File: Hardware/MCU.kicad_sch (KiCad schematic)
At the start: 30 parts, among them IC1 SN74AHC1G32DBVR, J3 SWD, SW1 RST, SW2 BOOT, U5 STM32L431CBTx, Y1 8M

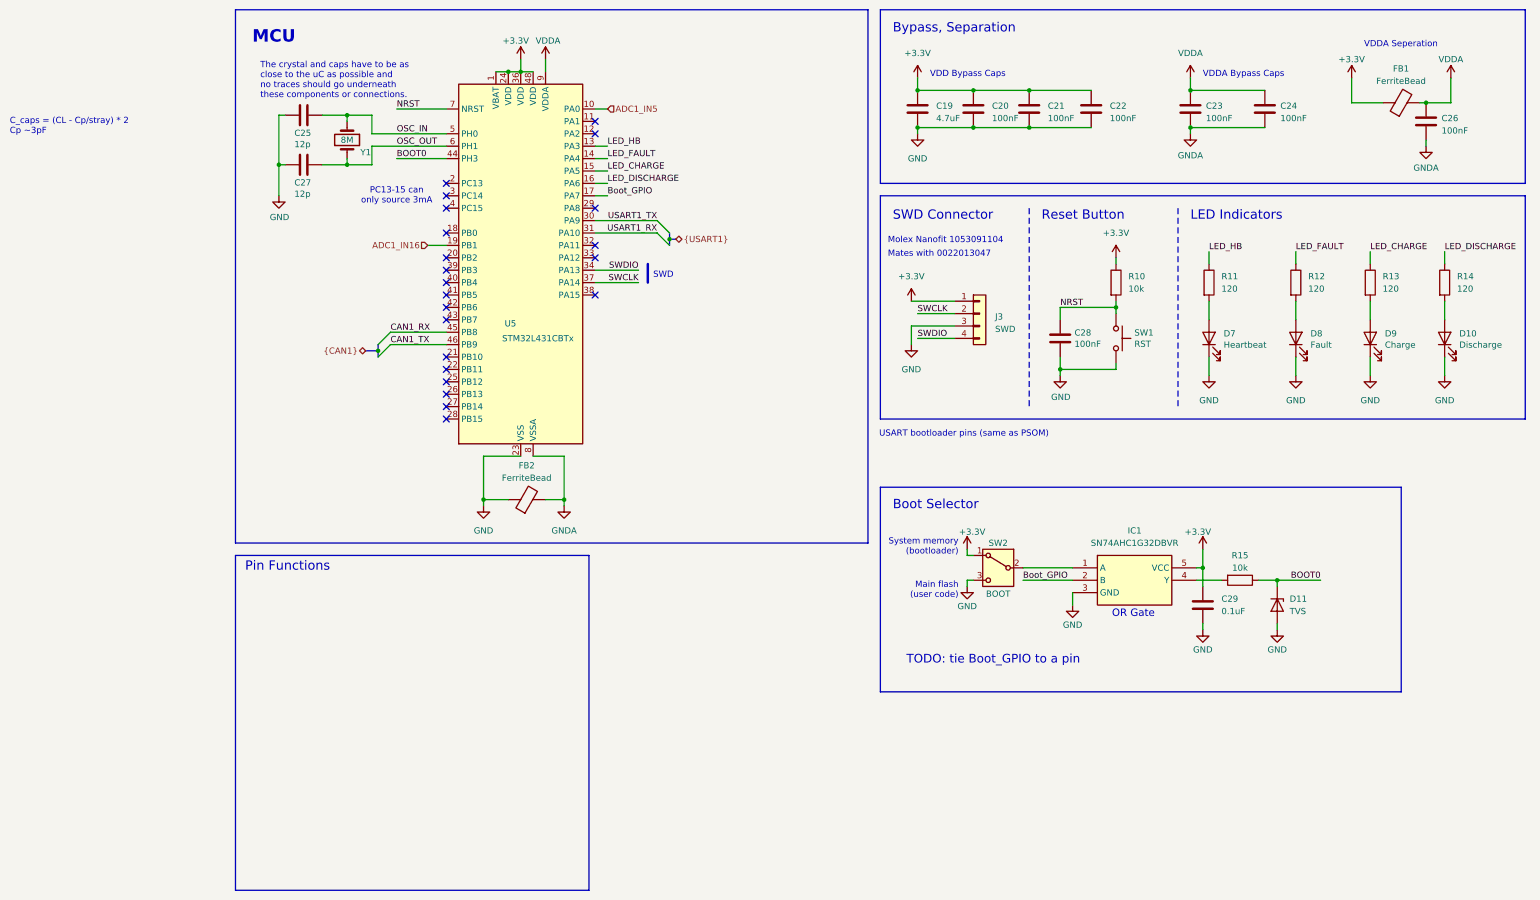
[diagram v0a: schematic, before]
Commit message: RevB Changes (#4)
* added documentation for current range; added VBUS led

* INA common-mode fixed (i think)

* differential amp for LPF

* diff amp / LPF

* some comments so I don't forget what I'm doing

* new TLV symbol, SPDT switch for scrut

* fixed LPF cutoff

* refactored and added LPF docs; added fuse, boot_gpio from USB-UART chip

* i lowk haven't started layout

* slightly cooked

* started layout not really but kind of

* layout stuff

* post review council sch changes: shielded connectors, removed SHDN resistor, diode OR for boot, standardized resistors

* starting routing i think

* almost done with routing

* wow

* drc is happy

* ye

* again

* addressed some comments

* added lcsc part numbers

* generated production files and docs

* updated STEP file

* symbol library

* addressed comments; generated production files, docs

* added Mouser BOM, deleted embedded step files
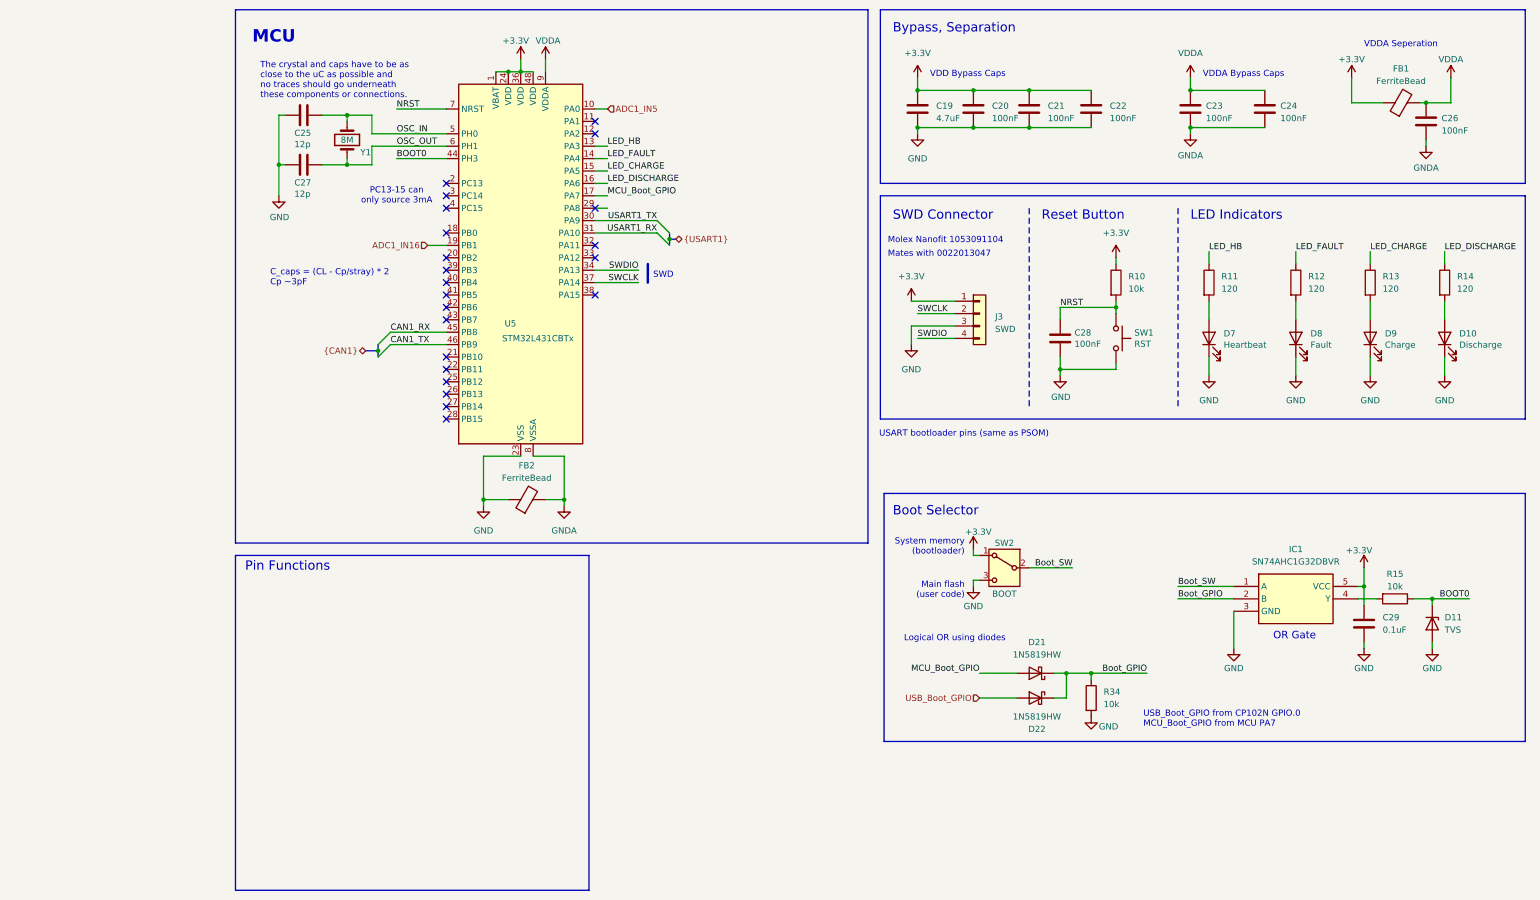
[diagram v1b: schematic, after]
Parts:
- added D21, D22: 1N5819HW, Diode_SMD:D_SOD-123, symbol Device:D_Schottky
- added R34: 10k, Resistor_SMD:R_0603_1608Metric_Pad0.98x0.95mm_HandSolder, symbol Device:R
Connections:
- net Boot_GPIO: now also D21.1 (K), D22.1 (K), R34.1; no longer U5.17 (PA7)
- net GND: now also R34.2
- net Boot_SW: now reaches IC1.1 (A), SW2.2 (B)
- new net MCU_Boot_GPIO: D21.2 (A), U5.17 (PA7)
- new net USB_Boot_GPIO: D22.2 (A)
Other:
- note added: "Logical OR using diodes"
- note added: "USB_Boot_GPIO from CP102N GPIO.0 MCU_Boot_GPIO from MCU PA7"
- note removed: "TODO: tie Boot_GPIO to a pin"
- moved on the sheet: C29, D11, IC1, R15, SW2
